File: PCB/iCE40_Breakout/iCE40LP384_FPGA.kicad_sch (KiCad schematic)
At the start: 31 parts, among them J1 Conn_01x08, J2 Conn_01x10, J3 Conn_01x10, Q1 L2N7002SLLT1G, SW1 KH-6X6X5H-STM, U1 ICE40LP384-SG32

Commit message: Updated all TPs to use pads, not holes for hooks. Also removed duplicate SPI programming TPs
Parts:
- TP1, TP2, TP3, TP4, TP5, TP6, TP7: footprint TestPoint:TestPoint_Loop_D1.80mm_Drill1.0mm_Beaded -> TestPoint:TestPoint_Pad_D1.0mm
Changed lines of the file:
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@@
 			)
 		)
-		(property "Footprint" "TestPoint:TestPoint_Loop_D1.80mm_Drill1.0mm_Beaded"
+		(property "Footprint" "TestPoint:TestPoint_Pad_D1.0mm"
 			(at 255.27 135.89 0)
 			(effects
@@
 			)
 		)
-		(property "Footprint" "TestPoint:TestPoint_Loop_D1.80mm_Drill1.0mm_Beaded"
+		(property "Footprint" "TestPoint:TestPoint_Pad_D1.0mm"
 			(at 255.27 140.97 0)
 			(effects
@@
 			)
 		)
-		(property "Footprint" "TestPoint:TestPoint_Loop_D1.80mm_Drill1.0mm_Beaded"
+		(property "Footprint" "TestPoint:TestPoint_Pad_D1.0mm"
 			(at 255.27 146.05 0)
 			(effects
@@
 			)
 		)
-		(property "Footprint" "TestPoint:TestPoint_Loop_D1.80mm_Drill1.0mm_Beaded"
+		(property "Footprint" "TestPoint:TestPoint_Pad_D1.0mm"
 			(at 255.27 143.51 0)
 			(effects
@@
 			)
 		)
-		(property "Footprint" "TestPoint:TestPoint_Loop_D1.80mm_Drill1.0mm_Beaded"
+		(property "Footprint" "TestPoint:TestPoint_Pad_D1.0mm"
 			(at 255.27 151.13 0)
 			(effects
@@
 			)
 		)
-		(property "Footprint" "TestPoint:TestPoint_Loop_D1.80mm_Drill1.0mm_Beaded"
+		(property "Footprint" "TestPoint:TestPoint_Pad_D1.0mm"
 			(at 255.27 148.59 0)
 			(effects
@@
 			)
 		)
-		(property "Footprint" "TestPoint:TestPoint_Loop_D1.80mm_Drill1.0mm_Beaded"
+		(property "Footprint" "TestPoint:TestPoint_Pad_D1.0mm"
 			(at 255.27 138.43 0)
 			(effects

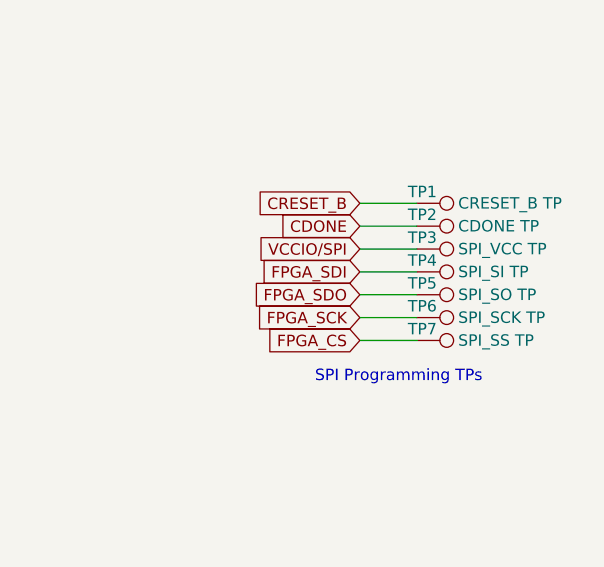
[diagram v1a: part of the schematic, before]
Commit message: Actually removed duplicate TPs from schematic this time
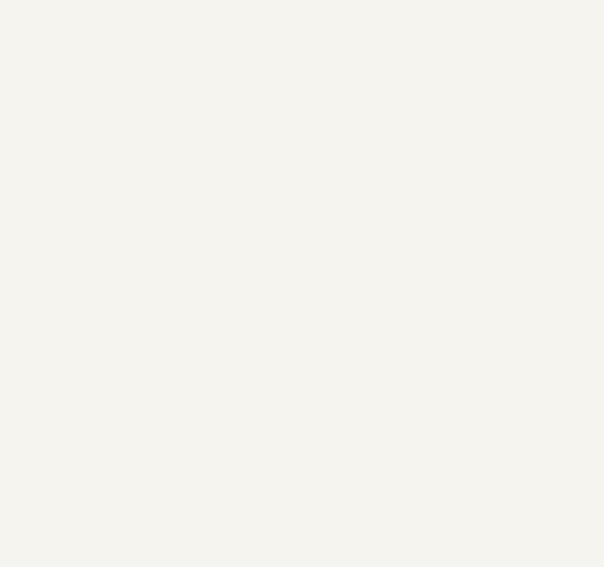
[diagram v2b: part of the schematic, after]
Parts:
- removed TP1: CRESET_B TP, TestPoint:TestPoint_Pad_D1.0mm, symbol Connector:TestPoint
- removed TP2: CDONE TP, TestPoint:TestPoint_Pad_D1.0mm, symbol Connector:TestPoint
- removed TP3: SPI_VCC TP, TestPoint:TestPoint_Pad_D1.0mm, symbol Connector:TestPoint
- removed TP4: SPI_SI TP, TestPoint:TestPoint_Pad_D1.0mm, symbol Connector:TestPoint
- removed TP5: SPI_SO TP, TestPoint:TestPoint_Pad_D1.0mm, symbol Connector:TestPoint
- removed TP6: SPI_SCK TP, TestPoint:TestPoint_Pad_D1.0mm, symbol Connector:TestPoint
- removed TP7: SPI_SS TP, TestPoint:TestPoint_Pad_D1.0mm, symbol Connector:TestPoint
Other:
- note removed: "SPI Programming TPs"

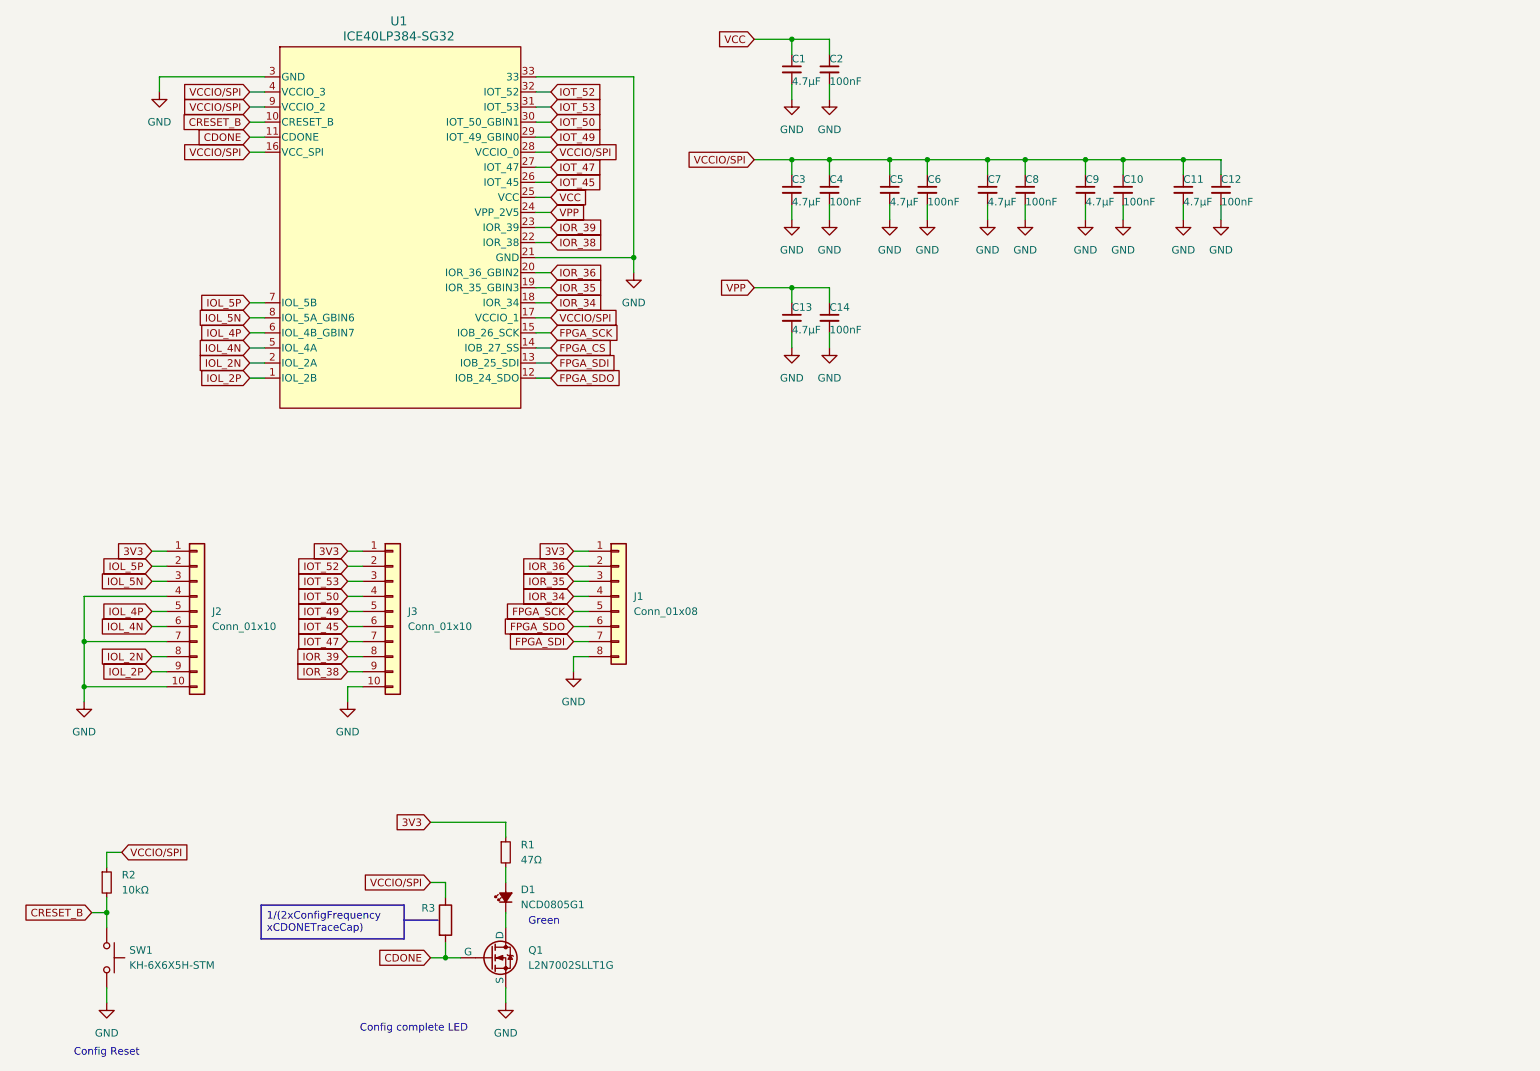
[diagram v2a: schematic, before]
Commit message: Rearranged GPIO pinouts to allow for easier wiring of the external GPIO headers
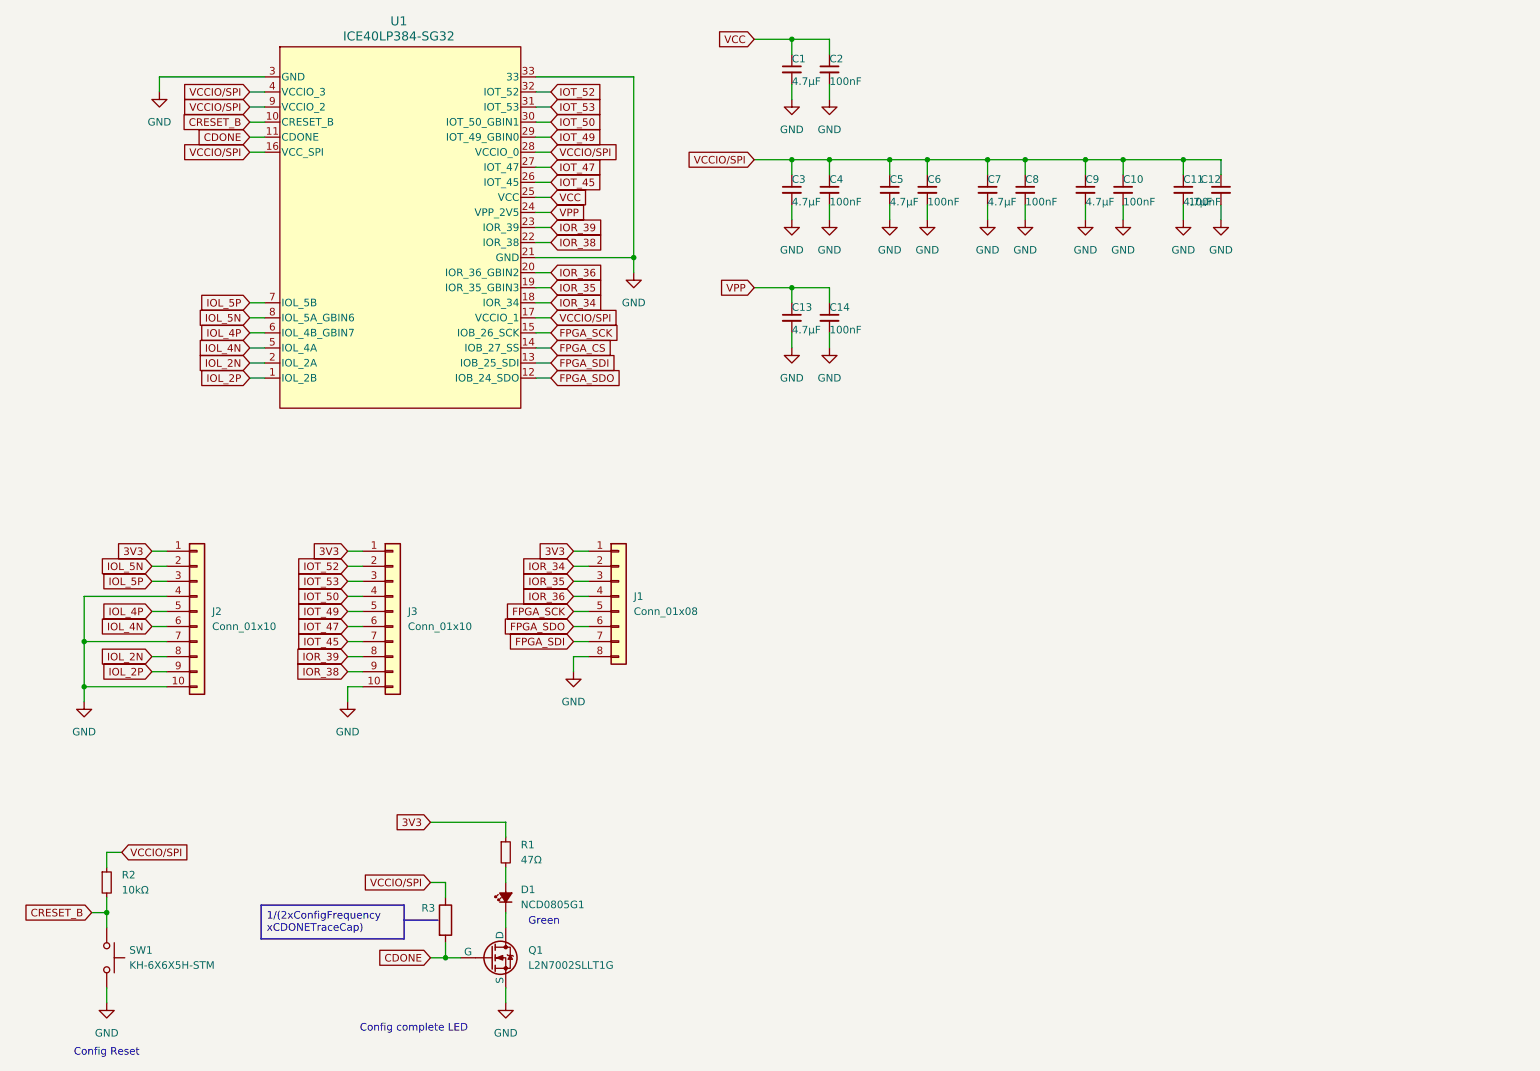
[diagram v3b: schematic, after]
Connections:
- net IOL_5N: now also J2.2 (Pin_2); no longer J2.3 (Pin_3)
- net IOL_5P: now also J2.3 (Pin_3); no longer J2.2 (Pin_2)
- net IOR_34: now also J1.2 (Pin_2); no longer J1.4 (Pin_4)
- net IOR_36: now also J1.4 (Pin_4); no longer J1.2 (Pin_2)
- net IOT_45: now also J3.7 (Pin_7); no longer J3.6 (Pin_6)
- net IOT_47: now also J3.6 (Pin_6); no longer J3.7 (Pin_7)

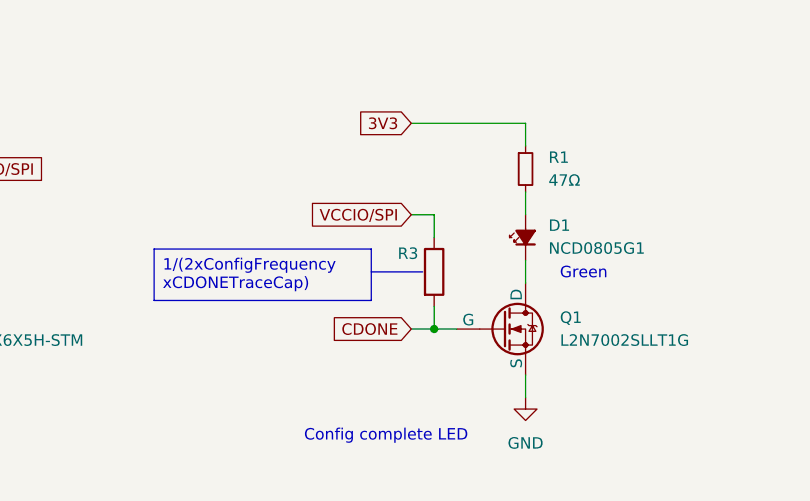
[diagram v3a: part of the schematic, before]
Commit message: Placed CDONE pullup as 10k, guessing a trace cap of ~10pF and rounding up
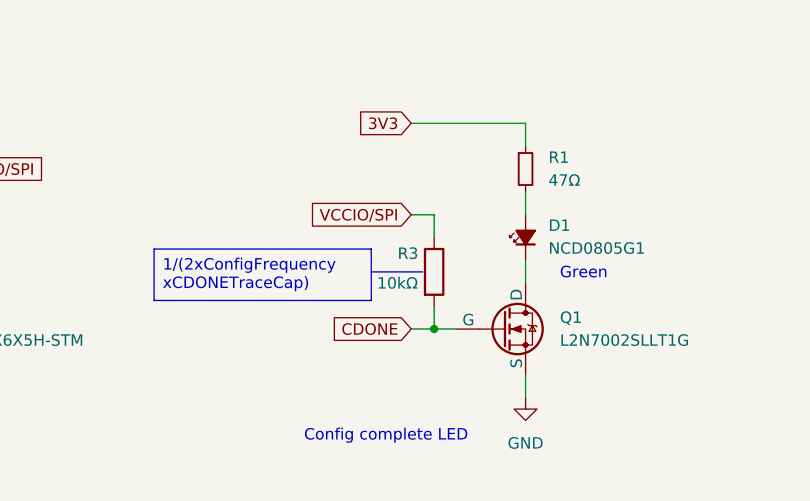
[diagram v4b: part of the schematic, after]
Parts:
- R3: LCSC (none) -> C25804
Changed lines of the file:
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@@
 		)
 		(property "Value" "10kΩ"
-			(at 93.98 173.9899 0)
+			(at 85.09 173.99 0)
 			(effects
 				(font
@@
 				)
 				(justify left)
-				(hide yes)
 			)
 		)
@@
 			(at 91.44 172.72 0)
 			(effects
+				(font
+					(size 1.27 1.27)
+				)
+				(hide yes)
+			)
+		)
+		(property "LCSC" "C25804"
+			(at 91.44 172.72 0)
+			(effects

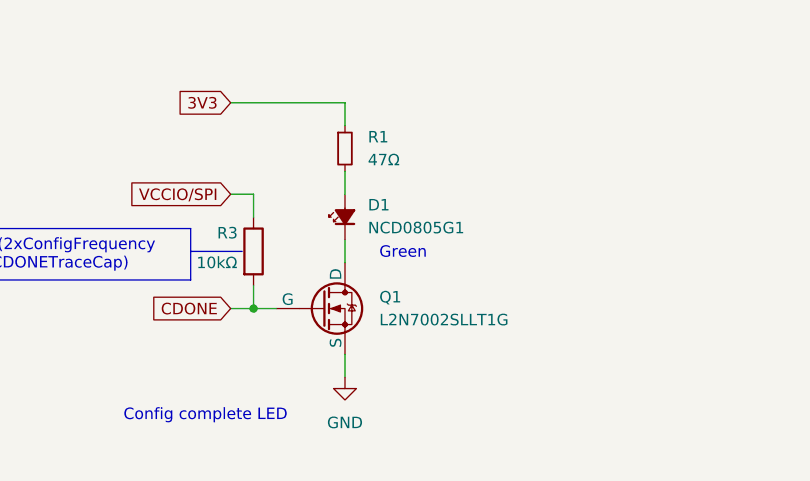
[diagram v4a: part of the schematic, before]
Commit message: Changed multiple caps, LEDs and NMOSs to JLCPCB basic parts
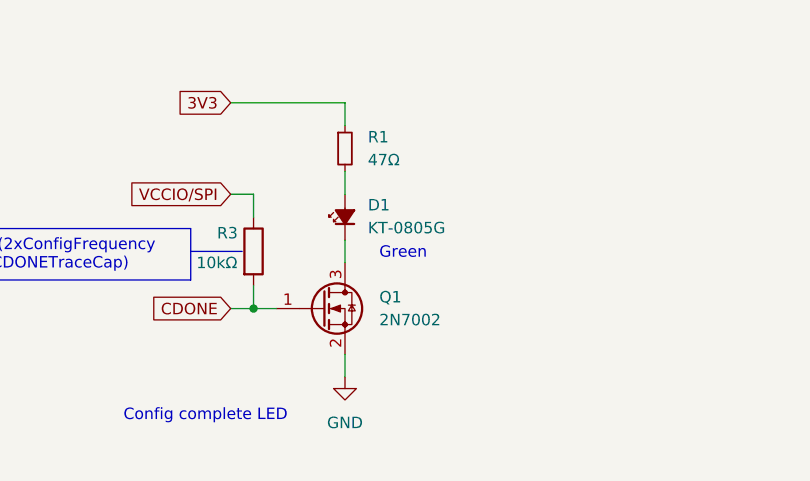
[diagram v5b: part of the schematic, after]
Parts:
- D1: value NCD0805G1 -> KT-0805G; LCSC C84260 -> C2297
- Q1: value L2N7002SLLT1G -> 2N7002; symbol Simulation_SPICE:NMOS -> Transistor_FET:2N7002; LCSC C22446827 -> C8545
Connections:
- net CDONE: now also Q1.1 (G); no longer Q1.2 (G)
- net GND: now also Q1.2 (S); no longer Q1.3 (S)
- net at D1.1 (K): now also Q1.3 (D); no longer Q1.1 (D)
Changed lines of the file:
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@@
 	)
 	(symbol
-		(lib_id "Simulation_SPICE:NMOS")
+		(lib_id "Transistor_FET:2N7002")
 		(at 99.06 179.07 0)
 		(unit 1)
@@
 			)
 		)
-		(property "Value" "L2N7002SLLT1G"
+		(property "Value" "2N7002"
 			(at 105.41 180.34 0)
 			(effects
@@
 		)
 		(property "Footprint" "Package_TO_SOT_SMD:SOT-23"
-			(at 104.14 176.53 0)
-			(effects
-				(font
-					(size 1.27 1.27)
-				)
-				(hide yes)
-			)
-		)
-		(property "Datasheet" ""
-			(at 99.06 191.77 0)
-			(effects
-				(font
-					(size 1.27 1.27)
-				)
-				(hide yes)
-			)
-		)
-		(property "Description" "N-MOSFET transistor, drain/source/gate"
+			(at 104.14 180.975 0)
+			(effects
+				(font
+					(size 1.27 1.27)
+					(italic yes)
+				)
+				(justify left)
+				(hide yes)
+			)
+		)
+		(property "Datasheet" "https://www.onsemi.com/pub/Collateral/NDS7002A-D.PDF"
+			(at 104.14 182.88 0)
+			(effects
+				(font
+					(size 1.27 1.27)
+				)
+				(justify left)
+				(hide yes)
+			)
+		)
+		(property "Description" "0.115A Id, 60V Vds, N-Channel MOSFET, SOT-23"
 			(at 99.06 179.07 0)
 			(effects
@@
 			)
 		)
-		(property "LCSC" "C22446827"
+		(property "LCSC" "C8545"
 			(at 99.06 179.07 0)
 			(effects
@@
 			)
 		)
-		(property "Value" "NCD0805G1"
+		(property "Value" "KT-0805G"
 			(at 104.14 170.1164 90)
 			(effects
@@
 			)
 		)
-		(property "LCSC" "C84260"
+		(property "LCSC" "C2297"
 			(at 101.6 168.91 90)
 			(effects
